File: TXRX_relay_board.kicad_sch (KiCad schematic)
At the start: 76 parts, among them J1 Screw_Terminal_01x02, J2 Conn_01x08, J3 IN, J4 IN_RF_Deck, J5 OUT_RF_Deck, J6 OUT, K1 RT314A05, K2 RT314A05, Q1 BC807, Q2 BC807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

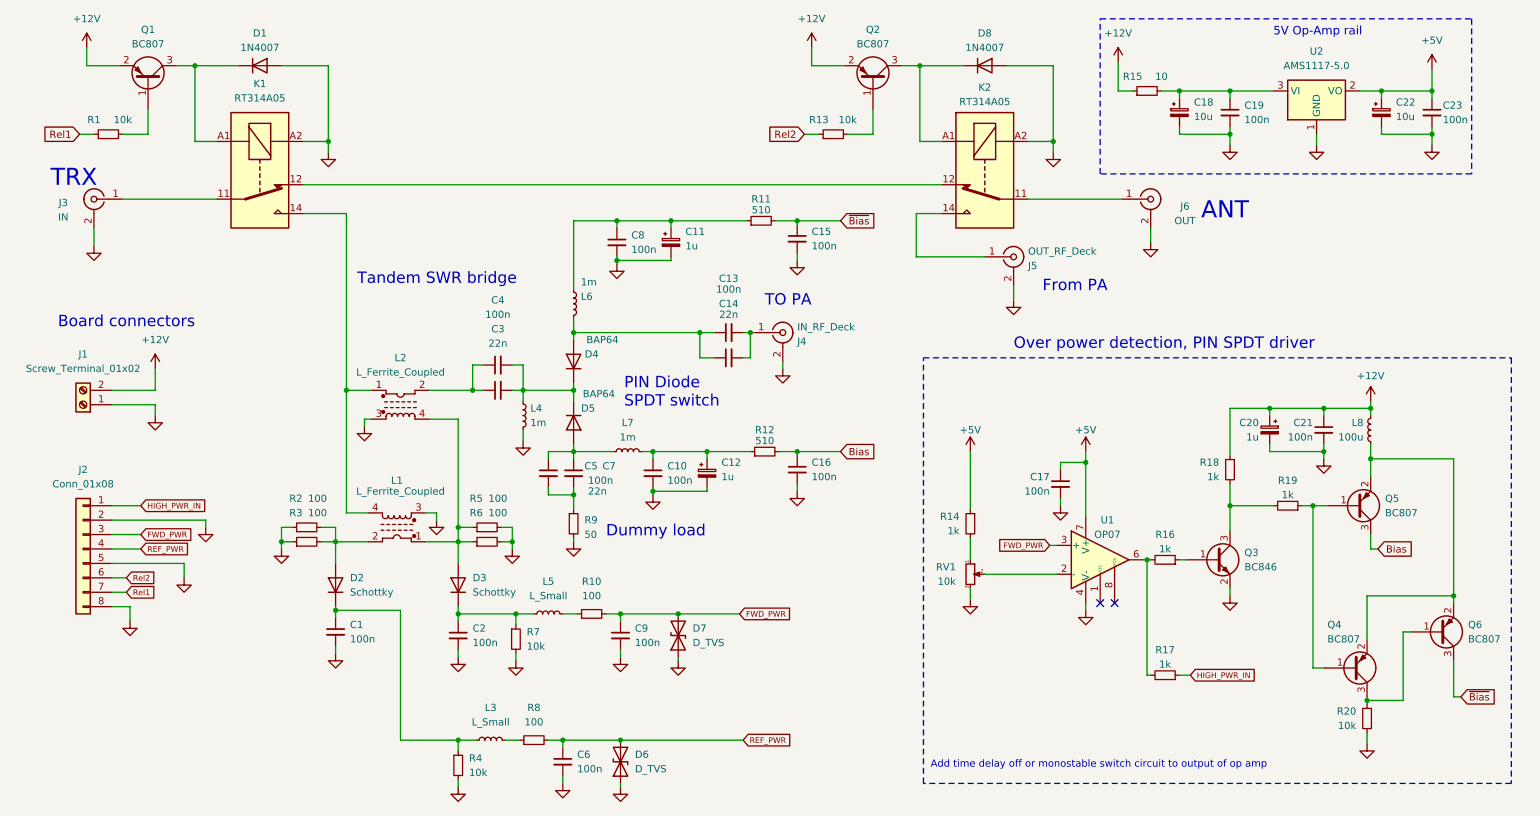
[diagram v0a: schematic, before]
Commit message: Used ERC to fix minor Errors
Used the ERC to fix minor error and warnings. Some relegated to "Excluded"
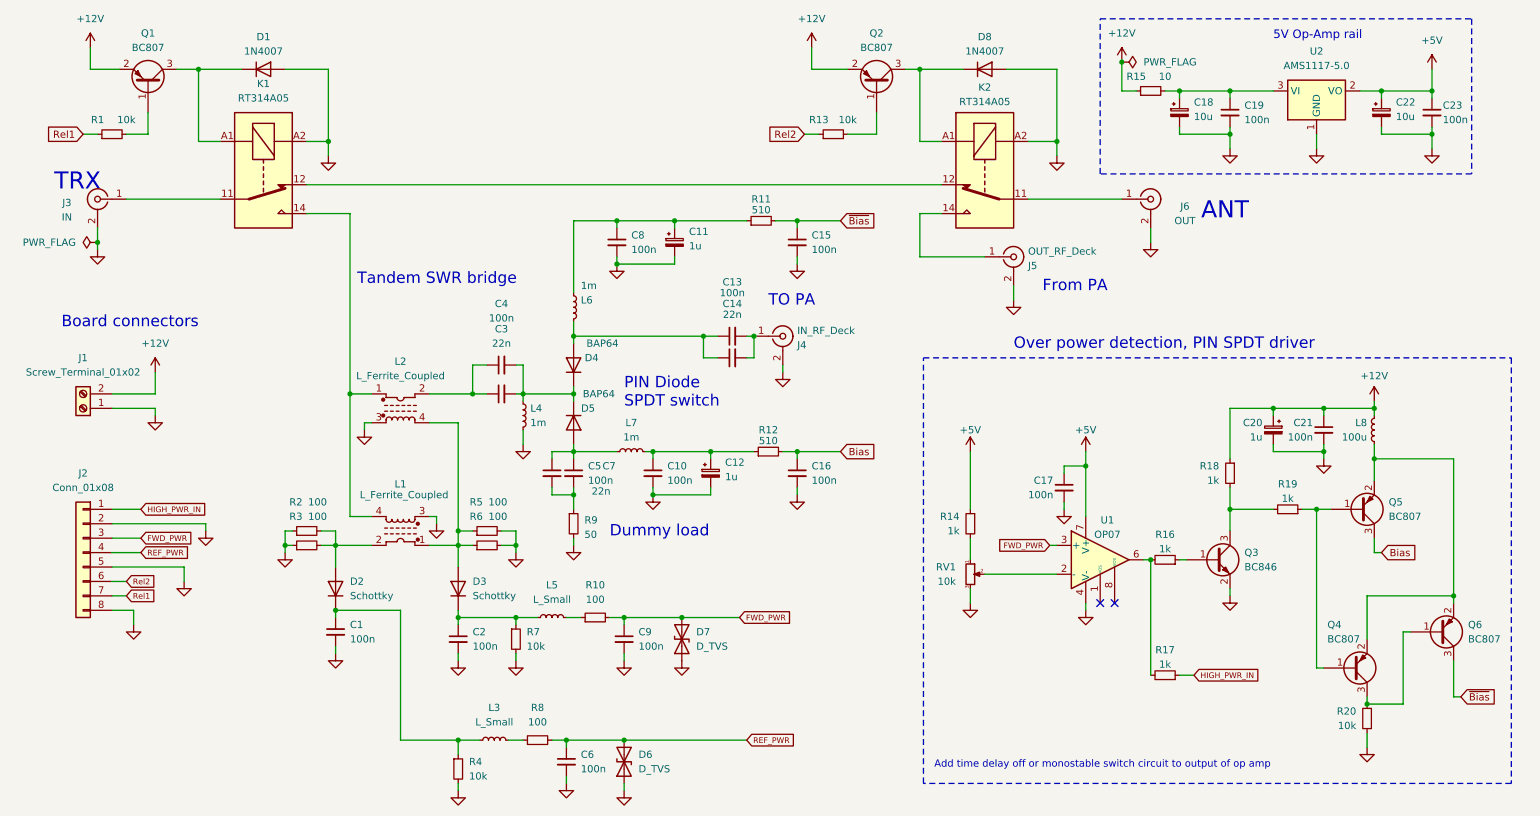
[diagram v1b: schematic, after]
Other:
- moved on the sheet: C11, C12, C13, C14, C15, C16, C17, C2, C20, C3, C4, C5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

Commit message: All checks done, BOM updated
All ERC and DRC checks have been run, and erros and or warnings resolved.
BOM fully updated with Manufacturer part numbers (MPN) ready for order placement
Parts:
- C1, C10, C15, C16, C17, C19, C2, C21, C23, C8, C9: MPN (none) -> MLASH168SB7104KTNA01; Pkg (none) -> SMD 0603; Ratings (none) -> 100V
- C11, C12, C20: MPN (none) -> HMR212CC7105KG-T; Pkg (none) -> SMD 0805; Ratings (none) -> 100V
- C13, C4, C6, C7: MPN (none) -> 08051C104KAT4A; Pkg (none) -> SMD 0805; Ratings (none) -> 100V
- C14, C3, C5: MPN (none) -> C0805C223M1RACAUTO; Pkg (none) -> SMD 0805; Ratings (none) -> 100V
- C18, C22: MPN (none) -> KGM21AR71C106MU; Pkg (none) -> SMD 0805; Ratings (none) -> 100V
- D1, D8: MPN (none) -> MRA4007T3G; Pkg (none) -> SMA 214AC
- D2, D3: value Schottky -> 1N4148; footprint Diode_SMD:D_SMA -> Diode_SMD:D_SOD-123F; MPN (none) -> 1N4148W-G3-08; Pkg (none) -> SMD-SOD-123
- D4, D5: MPN (none) -> BAP64-03,115; Pkg (none) -> SMD SOD-323
- D6, D7: footprint Diode_SMD:D_SOD-323 -> Diode_SMD:D_0805_2012Metric_Pad1.15x1.40mm_HandSolder; MPN (none) -> EZA-EGCA50AV; Pkg (none) -> SMD 0805; Ratings (none) -> 30v
- J1: MPN (none) -> 1548128; Pkg (none) -> Fixed Terminal Block
- J2: MPN (none) -> B8B-EH-A(LF)(SN)(P); Pkg (none) -> B8B-EH-A(LF)(SN)(P)
- J3, J4: MPN (none) -> 901-144-8RFX; Pkg (none) -> SMA - Vertical
- J5, J6: Pkg (none) -> Solder
- K1, K2: MPN (none) -> RT314A05; Pkg (none) -> THT
- L1: footprint TXRX_rel_lib:FT82_trafo -> TXRX_rel_lib:FT82-61_trafo; MPN (none) -> 5961000601; Pkg (none) -> Custom; Ratings (none) -> N>=15
- L2: footprint TXRX_rel_lib:FT82_trafo -> TXRX_rel_lib:FT50-61_trafo; MPN (none) -> 5961000301; Pkg (none) -> Custom; Ratings (none) -> N>=15
- L3, L5: value L_Small -> 1uH; MPN (none) -> ILSB0603ERR10K; Pkg (none) -> SMD 0603
- L4, L6, L7: value 1m -> 1mH; MPN (none) -> ISC1812ER102K; Pkg (none) -> SMD 1812; Ratings (none) -> 100V
- L8: value 100u -> 100uH; footprint Capacitor_SMD:C_1206_3216Metric_Pad1.33x1.80mm_HandSolder -> Inductor_SMD:L_1206_3216Metric; MPN (none) -> ILSB1206ER1R0K; Pkg (none) -> SMD 1206
- Q1, Q2, Q4, Q5, Q6: MPN (none) -> BC807-40-QVL; Pkg (none) -> SMD SOT-223-3
- Q3: MPN (none) -> BC846A; Pkg (none) -> SMD SOT-223-3
- R1, R13, R14, R16, R17, R18, R19, R20, R4, R7: MPN (none) -> RK73H1JTTDD1001F; Pkg (none) -> SMD 0603
- R10, R8: MPN (none) -> CRG0603F100R; Pkg (none) -> SMD 0603
- R11, R12: MPN (none) -> AC0603FR-07510RL; Pkg (none) -> SMD 1206
- R15: MPN (none) -> RNCL2010FT10R0; Pkg (none) -> SMD 2010; Ratings (none) -> 1.5W
- R2, R3, R5, R6: MPN (none) -> RMC1/2-101JTE; Pkg (none) -> SMD 2010
- R9: MPN (none) -> 901-144-8RFX; Pkg (none) -> SMA - Vertical; Ratings (none) -> Dummy Load
- RV1: MPN (none) -> 3296W-1-103; Pkg (none) -> THT xxxx
- U1: MPN (none) -> OP-07DPSR; Pkg (none) -> SO-SOIC
- U2: MPN (none) -> LM1117MPX-5.0/NOPB; Pkg (none) -> SMD SOT-223-3
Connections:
- net GND: now also K1.A1; no longer K1.A2
- net at D1.1 (K), Q1.3 (C): now also K1.A2; no longer K1.A1
